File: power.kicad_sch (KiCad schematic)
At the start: 26 parts, among them J201 Barrel_Jack_MountingPin, Q201 AOD4185, U101 74HC04, U102 74HC08, U103 74HC32, U51 TPS5430DDA

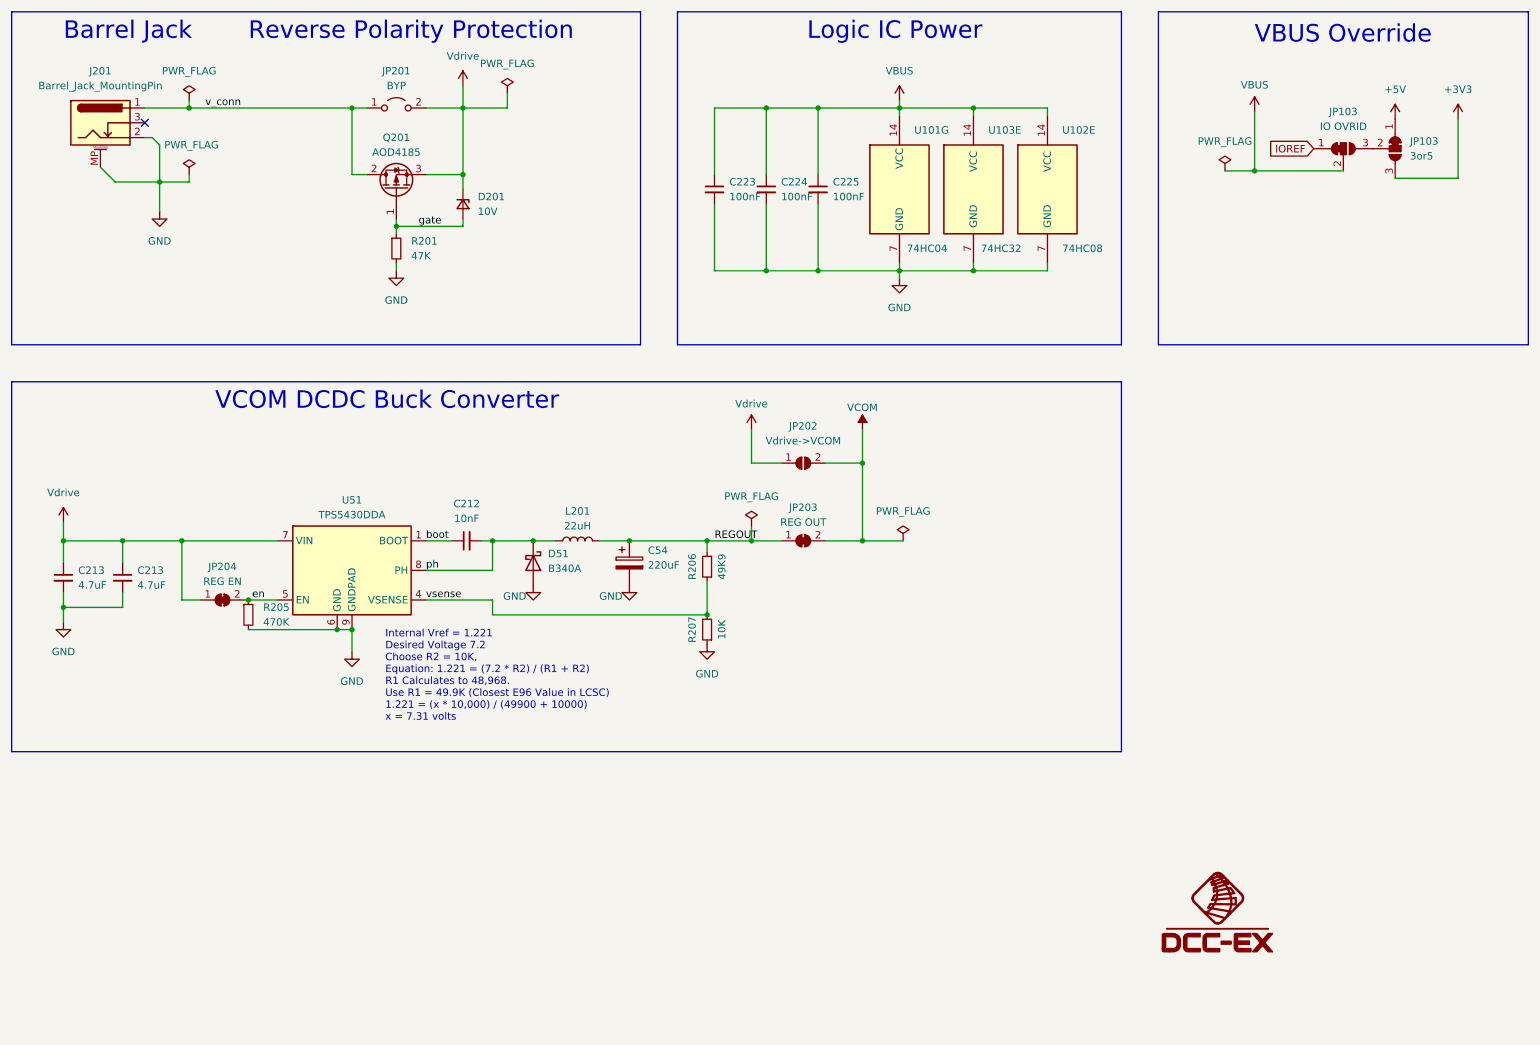
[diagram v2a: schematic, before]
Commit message: Reworked schematic to include an ESP32-S2-MINI-2.
Reworked schematic to include an ESP32-S2-MINI-2 as the main CPU.

Two track outputs are directly on this board.  The rest of the GPIO
pins are routed so that the existing EX-MotorShield8874 can stack.
The result is potentially 6 power outputs from a single unit.

Added a USB interface to the module.

Moved the drivers into heirarchal sheets.

Removed all unnecessary components.

Added a JTAG header for debugging.
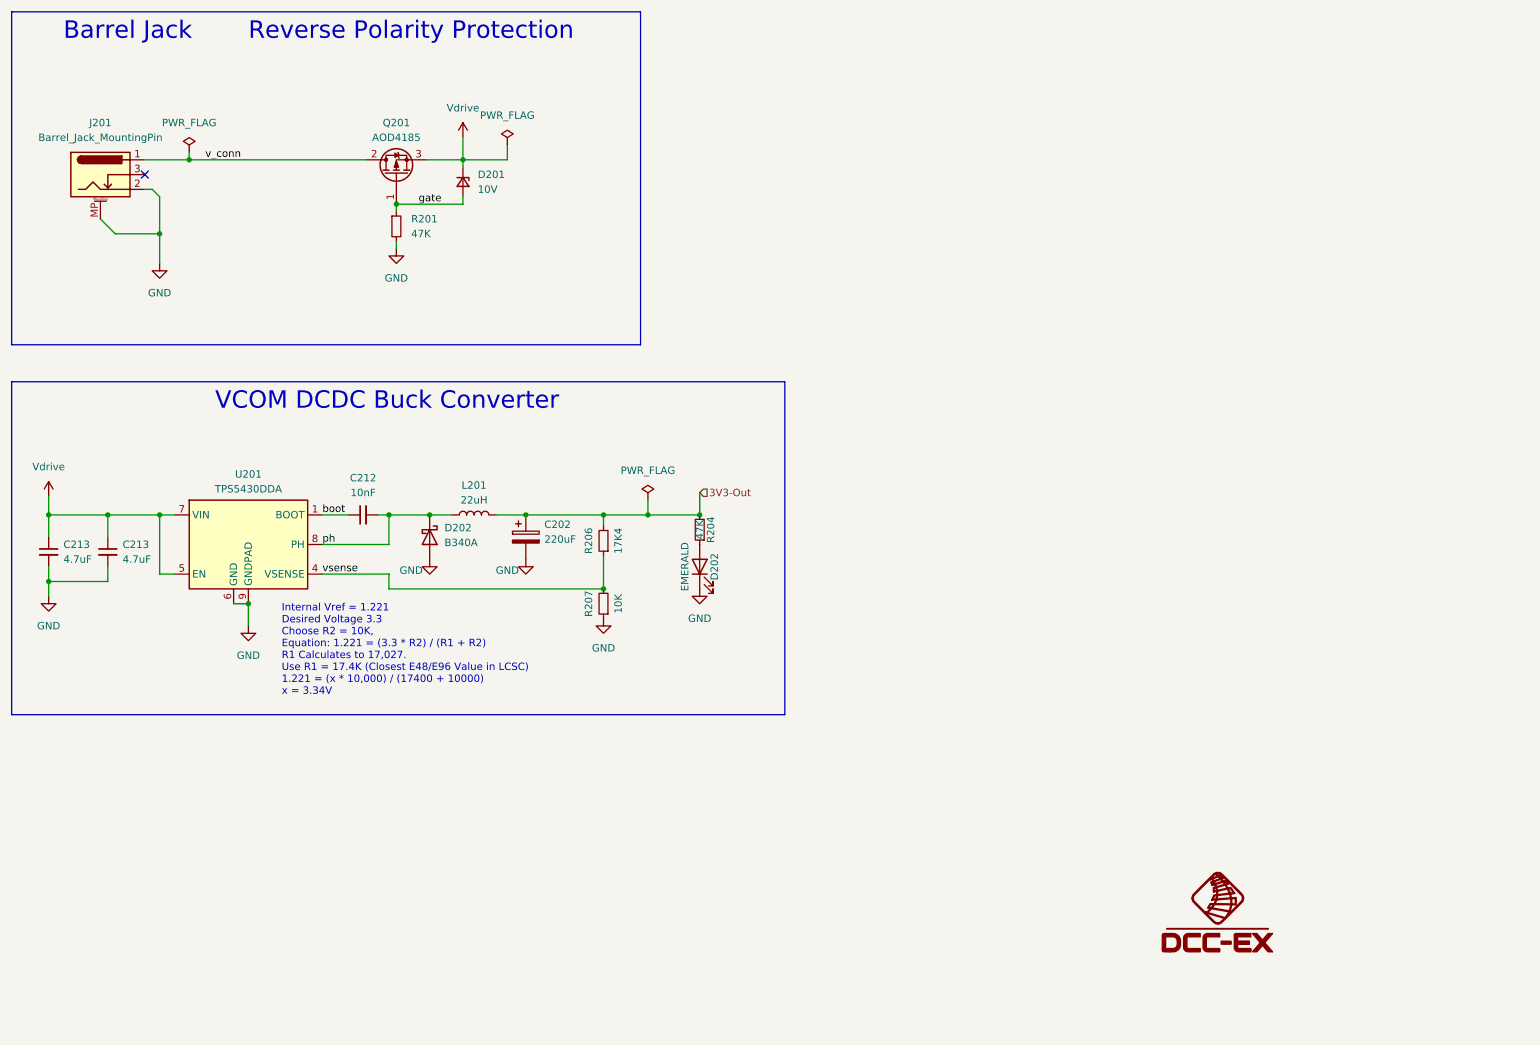
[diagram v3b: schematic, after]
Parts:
- removed C223, C224, C225: 100nF, Capacitor_SMD:C_0402_1005Metric, symbol Device:C_Small
- removed JP103: IO OVRID, Jumper:SolderJumper-3_P1.3mm_Bridged12_RoundedPad1.0x1.5mm, symbol Jumper:SolderJumper_3_Bridged12
- removed JP103: 3or5, Jumper:SolderJumper-3_P1.3mm_Bridged12_RoundedPad1.0x1.5mm, symbol Jumper:SolderJumper_3_Bridged12
- removed JP201: BYP, Jumper:SolderJumper-2_P1.3mm_Open_RoundedPad1.0x1.5mm, symbol Jumper:Jumper_2_Open
- removed JP202: Vdrive->VCOM, Jumper:SolderJumper-2_P1.3mm_Open_RoundedPad1.0x1.5mm, symbol Jumper:SolderJumper_2_Open
- removed JP203: REG OUT, Jumper:SolderJumper-2_P1.3mm_Bridged_RoundedPad1.0x1.5mm, symbol Jumper:SolderJumper_2_Bridged
- removed JP204: REG EN, Jumper:SolderJumper-2_P1.3mm_Bridged_RoundedPad1.0x1.5mm, symbol Jumper:SolderJumper_2_Bridged
- removed R205: 470K, Resistor_SMD:R_0402_1005Metric, symbol Device:R_Small
- removed U101: 74HC04, Package_SO:TSSOP-14_4.4x5mm_P0.65mm, symbol 74xx:74HC04
- removed U102: 74HC08, Package_SO:TSSOP-14_4.4x5mm_P0.65mm, symbol 74xx:74LS08
- removed U103: 74HC32, Package_SO:TSSOP-14_4.4x5mm_P0.65mm, symbol 74xx:74LS32
- added D202: EMERALD, LED_SMD:LED_0603_1608Metric, symbol Device:LED
- added R204: 47K, Resistor_SMD:R_0402_1005Metric, symbol Device:R_Small
- R206: value 49K9 -> 17K4; LCSC Part # C25897 -> C270636; MPN (none) -> 0402WGF174JTCE; Manufacturer (none) -> Uni-Royal; Substitute (none) -> Yes
- renumbered C54 to C202, D51 to D202, U51 to U201
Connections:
- net en is gone; now on net Vdrive: U201.5 (EN)
- net GND: now also D202.1 (K)
- net REGOUT renamed 3V3-Out
- net 3V3-Out: now also R204.2
- new net: D202.2 (A), R204.1
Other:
- note added: "Internal Vref = 1.221 Desired Voltage 3.3 Choose R2 = 10K, Equation: 1.221 = (3.3 * R2) / (R1 + R2) R1 Calculates to 17,027. Use R1 = 17.4K (Closest E48/E96 Value in LCSC) 1.221 = (x * 10,000) / (17400 + 10000) x = 3.34V"
- note removed: "Internal Vref = 1.221 Desired Voltage 7.2 Choose R2 = 10K, Equation: 1.221 = (7.2 * R2) / (R1 + R2) R1 Calculates to 48,968. Use R1 = 49.9K (Closest E96 Value in LCSC) 1.221 = (x * 10,000) / (49900 + 10000) x = 7.31 volts"
- note removed: "Logic IC Power"
- note removed: "VBUS Override"
- moved on the sheet: C202, C212, C213, D201, D202, J201, L201, Q201, R201, R206, R207, U201
